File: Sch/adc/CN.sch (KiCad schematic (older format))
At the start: 8 parts, among them J1 JP4, J2 Header5, P1 CONN_02X40, U1 LTC2292

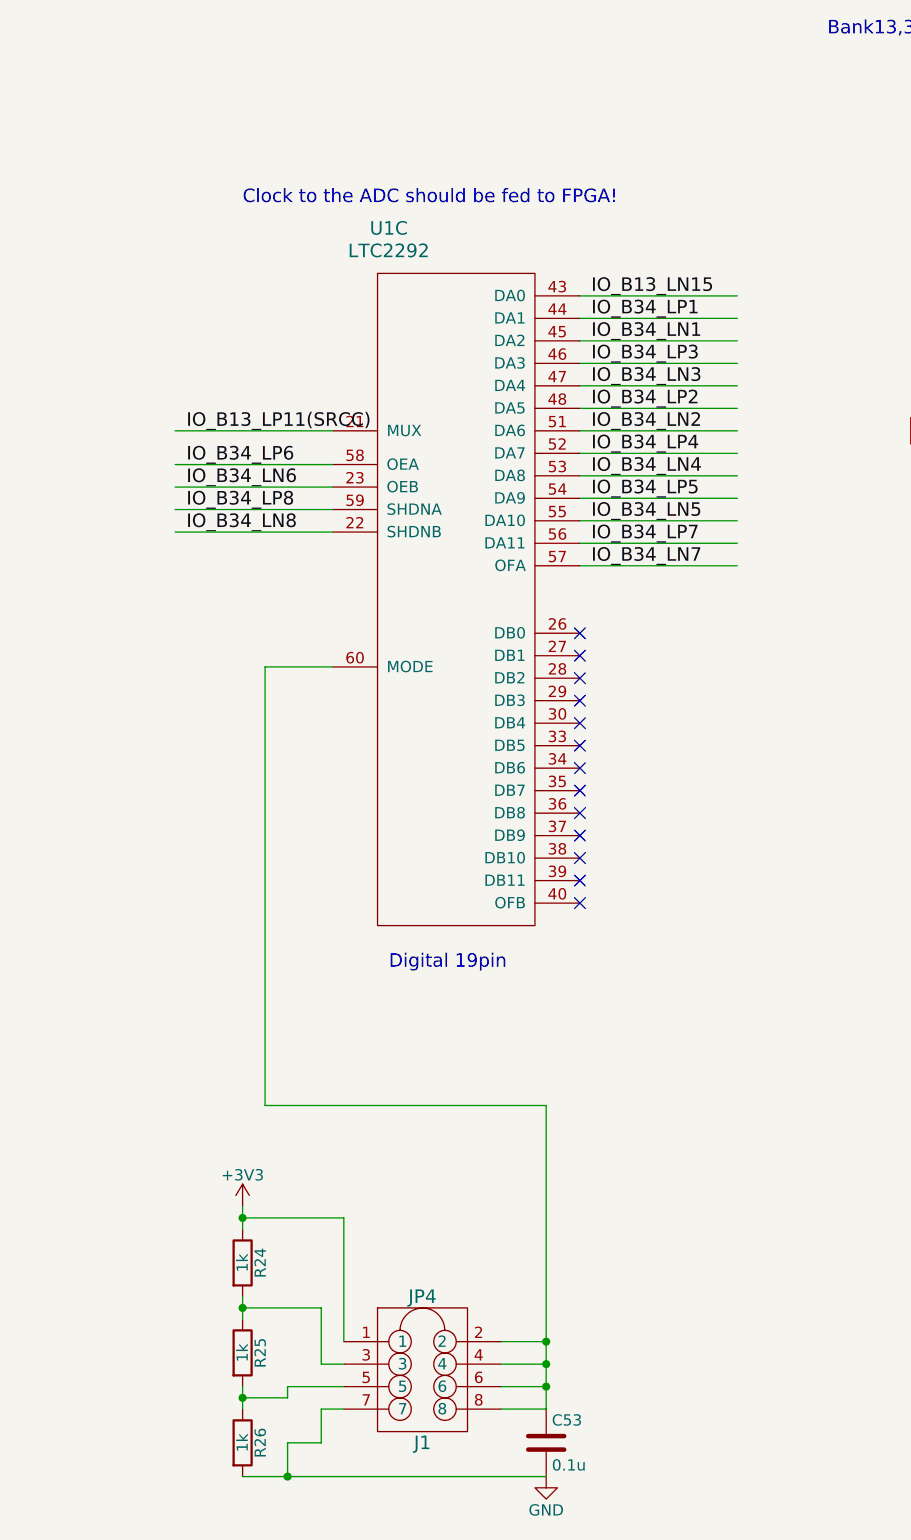
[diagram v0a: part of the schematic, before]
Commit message: Add resistors for ADC out
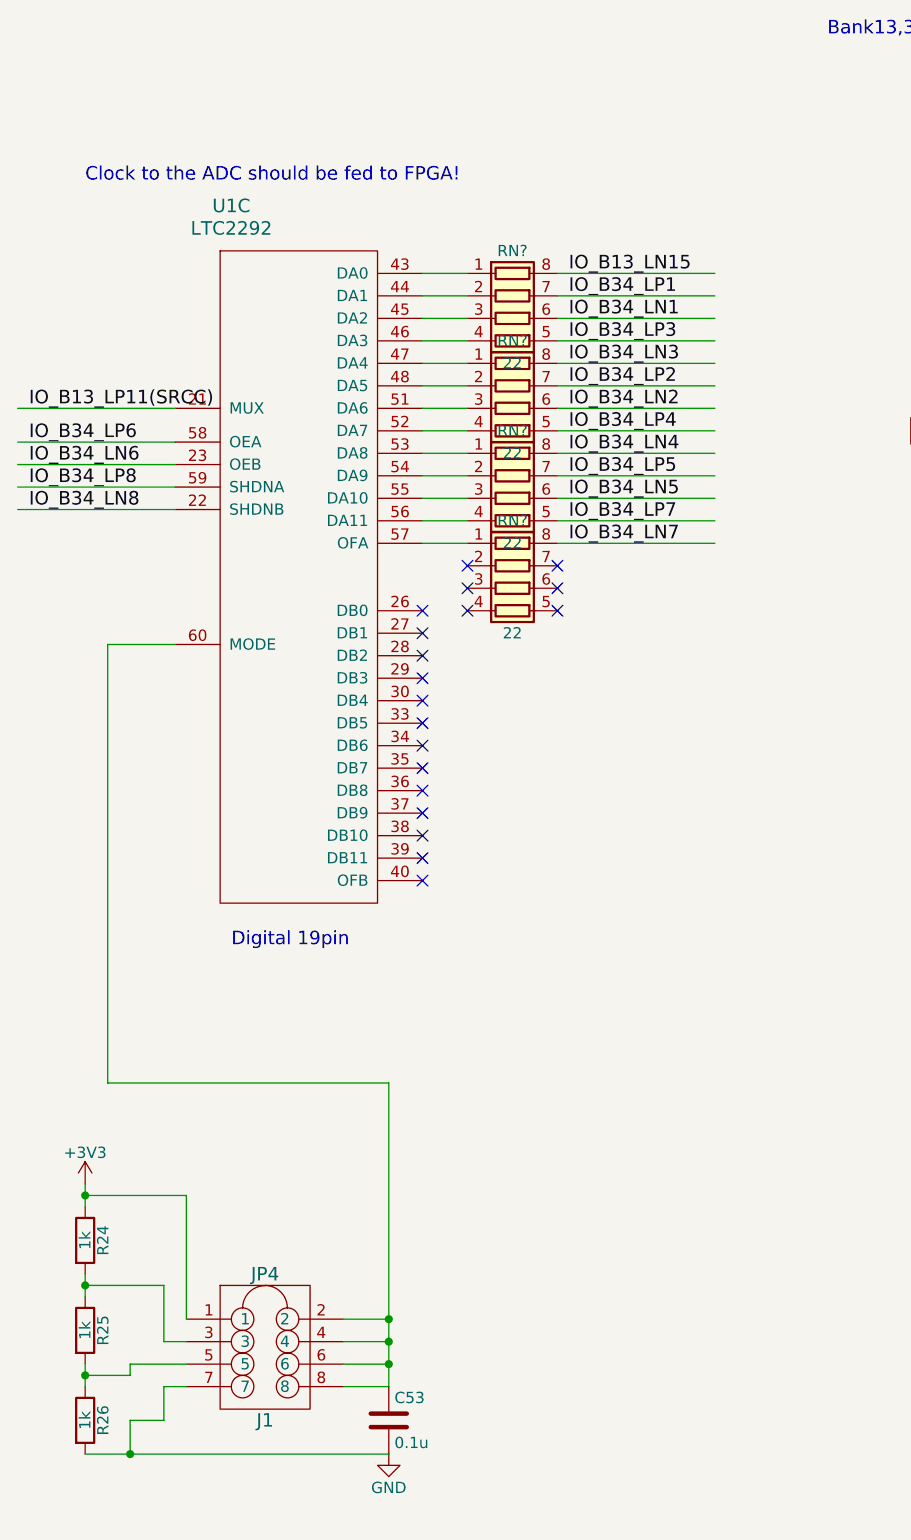
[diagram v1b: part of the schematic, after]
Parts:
- added RN? (x4): 22, symbol R_Pack04
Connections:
- wire segments 96 -> 109
- no-connect marks 55 -> 61
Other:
- moved on the sheet: C53, J1, R24, R25, R26, U1C

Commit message: Almost finished except Audio
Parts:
- gave numbers to parts that had none: 4
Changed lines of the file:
@@
 NoConn ~ 5950 2250
 $Comp
-L R_Pack04 RN?
+L R_Pack04 RN1
 U 1 1 58A5BF52
 P 3700 2050
-F 0 "RN?" V 3400 2050 50  0000 C CNN
+F 0 "RN1" V 3400 2050 50  0000 C CNN
 F 1 "22" V 3900 2050 50  0000 C CNN
 F 2 "" V 3975 2050 50  0001 C CNN
@@
 $EndComp
 $Comp
-L R_Pack04 RN?
+L R_Pack04 RN2
 U 1 1 58A5BFD7
 P 3700 2450
-F 0 "RN?" V 3400 2450 50  0000 C CNN
+F 0 "RN2" V 3400 2450 50  0000 C CNN
 F 1 "22" V 3900 2450 50  0000 C CNN
 F 2 "" V 3975 2450 50  0001 C CNN
@@
 $EndComp
 $Comp
-L R_Pack04 RN?
+L R_Pack04 RN3
 U 1 1 58A5C027
 P 3700 2850
-F 0 "RN?" V 3400 2850 50  0000 C CNN
+F 0 "RN3" V 3400 2850 50  0000 C CNN
 F 1 "22" V 3900 2850 50  0000 C CNN
 F 2 "" V 3975 2850 50  0001 C CNN
@@
 $EndComp
 $Comp
-L R_Pack04 RN?
+L R_Pack04 RN4
 U 1 1 58A5C02D
 P 3700 3250
-F 0 "RN?" V 3400 3250 50  0000 C CNN
+F 0 "RN4" V 3400 3250 50  0000 C CNN
 F 1 "22" V 3900 3250 50  0000 C CNN
 F 2 "" V 3975 3250 50  0001 C CNN

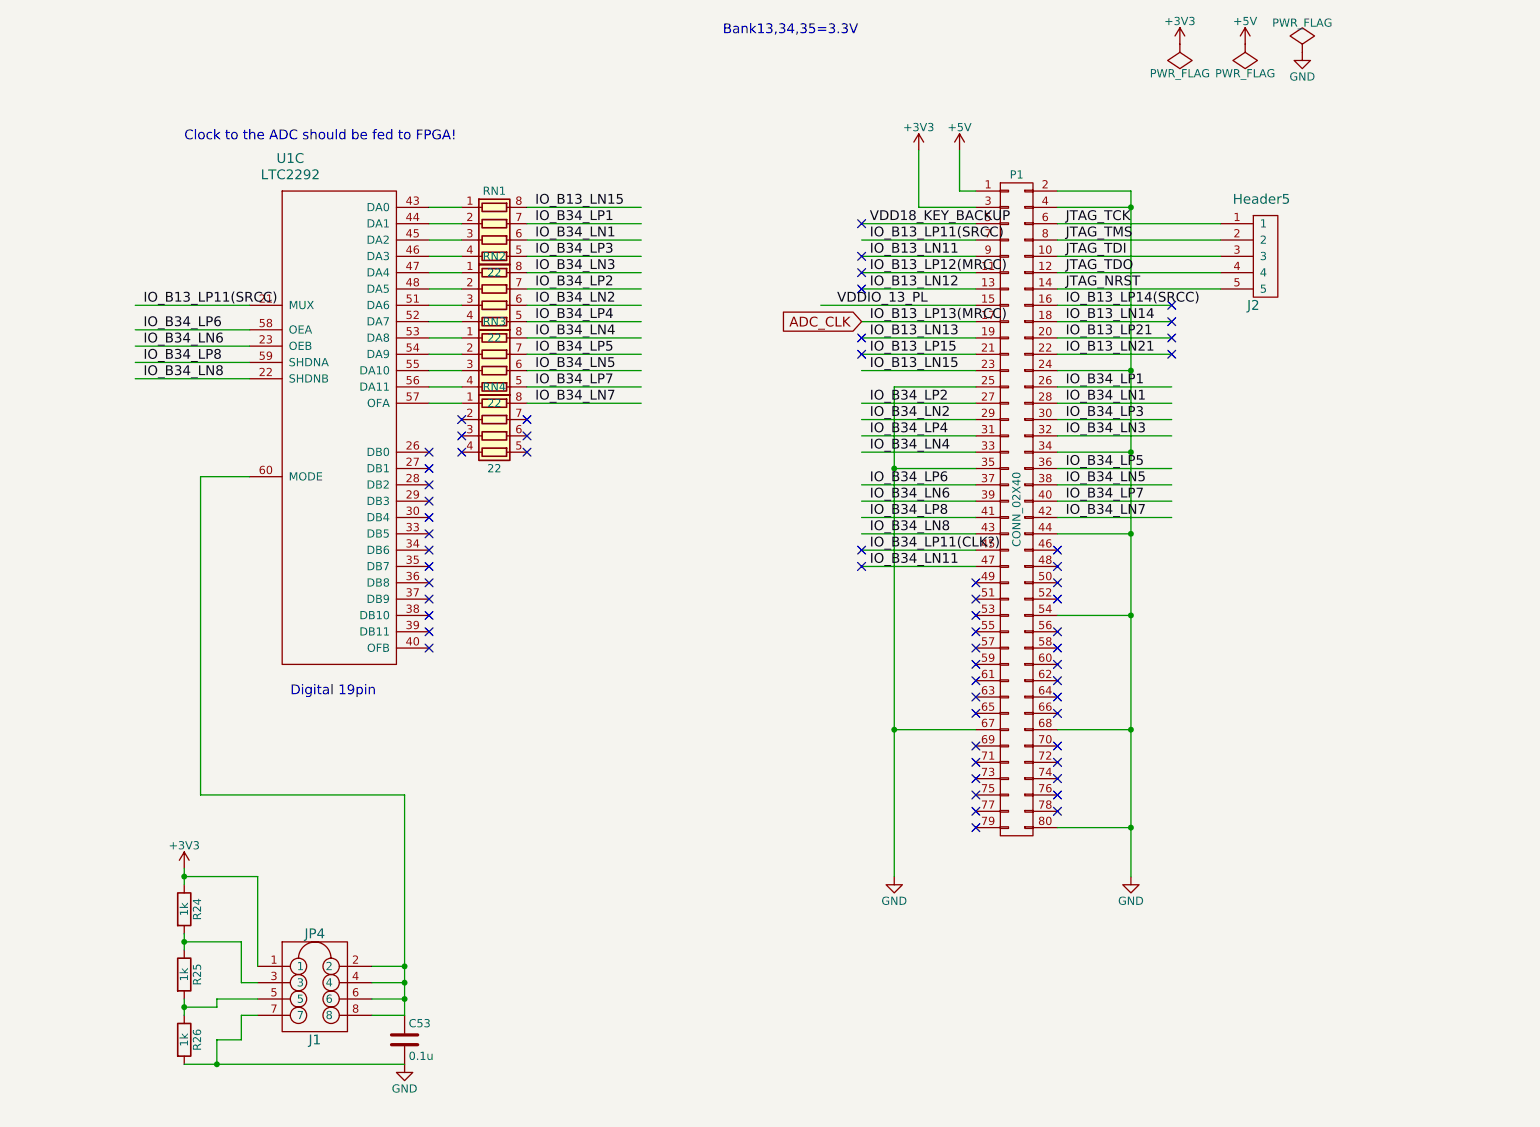
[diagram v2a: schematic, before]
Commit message: Fix MODE pin voltage of the ADC
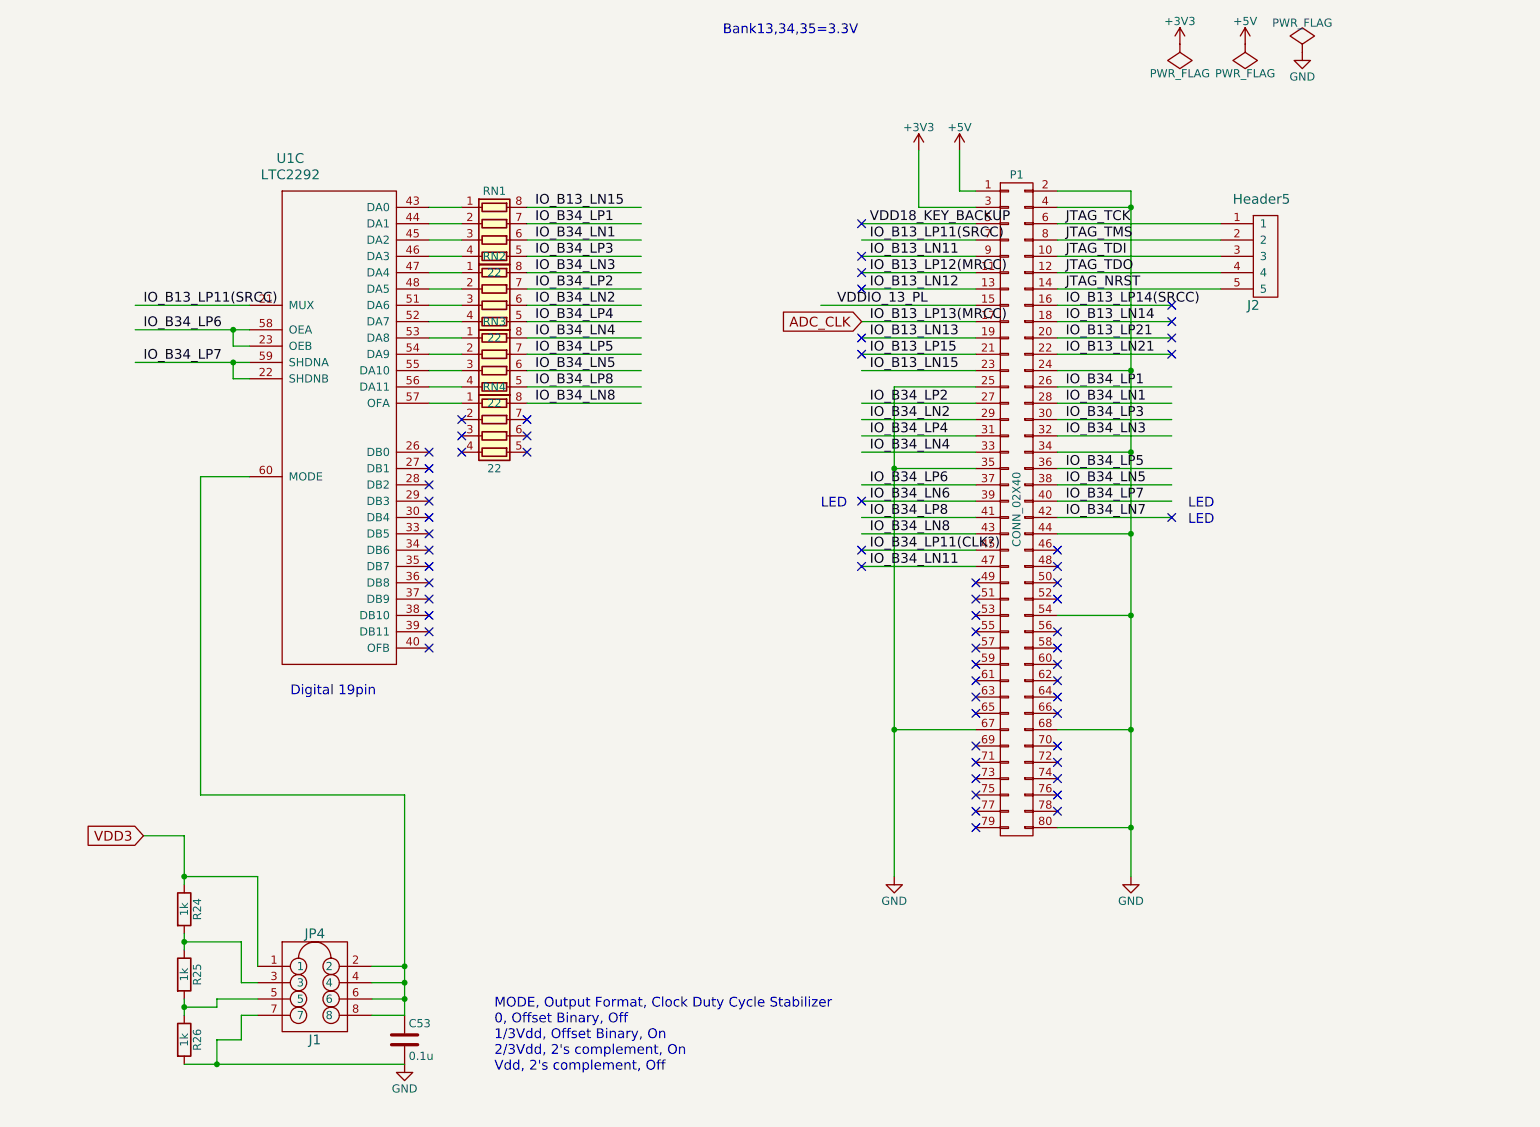
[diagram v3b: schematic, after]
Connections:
- net labels added: VDD3
- wire segments 109 -> 112
- no-connect marks 61 -> 63
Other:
- note added: "LED"
- note added: "MODE, Output Format, Clock Duty Cycle Stabilizer\n0, Offset Binary, Off\n1/3Vdd, Offset Binary, On\n2/3Vdd, 2's complement, On\nVdd, 2's complement, Off"
- note removed: "Clock to the ADC should be fed to FPGA!"
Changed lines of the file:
@@
 NoConn ~ 3300 4450
 NoConn ~ 3300 4550
-Text Notes 1800 1450 0    60   ~ 0
-Clock to the ADC should be fed to FPGA!
 Text Notes 2450 4850 0    60   ~ 0
 Digital 19pin
@@
 IO_B34_LN5
 Text Label 3950 2950 0    60   ~ 0
-IO_B34_LP7
+IO_B34_LP8
 Text Label 3950 3050 0    60   ~ 0
-IO_B34_LN7
+IO_B34_LN8
 Text Label 3950 2650 0    60   ~ 0
 IO_B34_LN4
@@
 Text Label 3950 1850 0    60   ~ 0
 IO_B13_LN15
-Text Label 1550 2900 0    60   ~ 0
-IO_B34_LN8
 Text Label 1550 2800 0    60   ~ 0
-IO_B34_LP8
-Text Label 1550 2700 0    60   ~ 0
-IO_B34_LN6
+IO_B34_LP7
 Text Label 1550 2600 0    60   ~ 0
 IO_B34_LP6
@@
 IO_B13_LP11(SRCC)
 $Comp
-L +3V3 #PWR011
-U 1 1 58A5E943
-P 1800 5900
-F 0 "#PWR011" H 1800 5750 50  0001 C CNN
-F 1 "+3V3" H 1800 6040 50  0000 C CNN
-F 2 "" H 1800 5900 50  0000 C CNN
-F 3 "" H 1800 5900 50  0000 C CNN
-	1    1800 5900
-	1    0    0    -1
-$EndComp
-$Comp
 L R R24
 U 1 1 58A5E977
@@
 $EndComp
 $Comp
-L GND #PWR012
+L GND #PWR011
 U 1 1 58A5EE0A
 P 3150 7100
-F 0 "#PWR012" H 3150 6850 50  0001 C CNN
+F 0 "#PWR011" H 3150 6850 50  0001 C CNN
 F 1 "GND" H 3150 6950 50  0000 C CNN
 F 2 "" H 3150 7100 50  0000 C CNN
@@
 	2200 2600 1500 2600
 Wire Wire Line
-	2200 2700 1500 2700
-Wire Wire Line
 	2200 2800 1500 2800
 Wire Wire Line
-	2200 2900 1500 2900
-Wire Wire Line
 	2200 2450 1500 2450
 Wire Wire Line
-	1800 5900 1800 6000
+	1800 5700 1800 6000
 Wire Wire Line
 	1800 6300 1800 6400
@@
 NoConn ~ 3900 3250
 NoConn ~ 3900 3150
+Wire Wire Line
+	2100 2800 2100 2900
+Wire Wire Line
+	2100 2900 2200 2900
+Connection ~ 2100 2800
+Wire Wire Line
+	2100 2600 2100 2700
+Wire Wire Line
+	2100 2700 2200 2700
+Connection ~ 2100 2600
+Text Notes 7950 3800 0    60   ~ 0
+LED
+Text Notes 7950 3700 0    60   ~ 0
+LED
+Text Notes 5700 3700 0    60   ~ 0
+LED
+NoConn ~ 5950 3650
+NoConn ~ 7850 3750
+Text Notes 3700 7150 0    60   ~ 0
+MODE, Output Format, Clock Duty Cycle Stabilizer\n0, Offset Binary, Off\n1/3Vdd, Offset Binary, On\n2/3Vdd, 2's complement, On\nVdd, 2's complement, Off
+Text GLabel 1550 5700 0    60   Input ~ 0
+VDD3
+Wire Wire Line
+	1550 5700 1800 5700
 $EndSCHEMATC

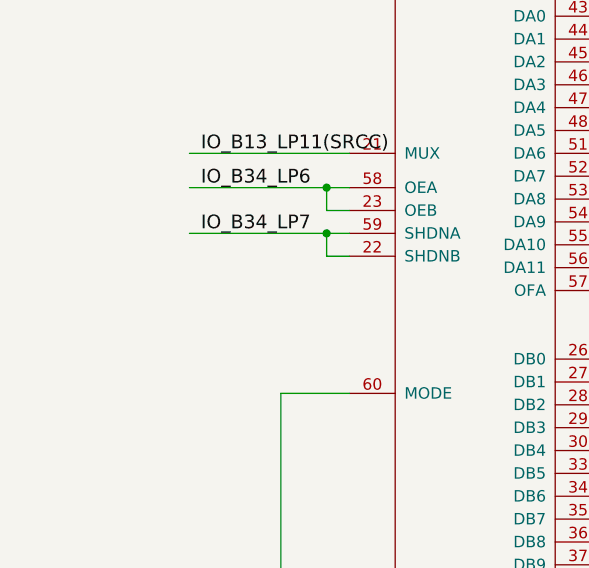
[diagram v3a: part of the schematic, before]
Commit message: Select nap mode for each channel
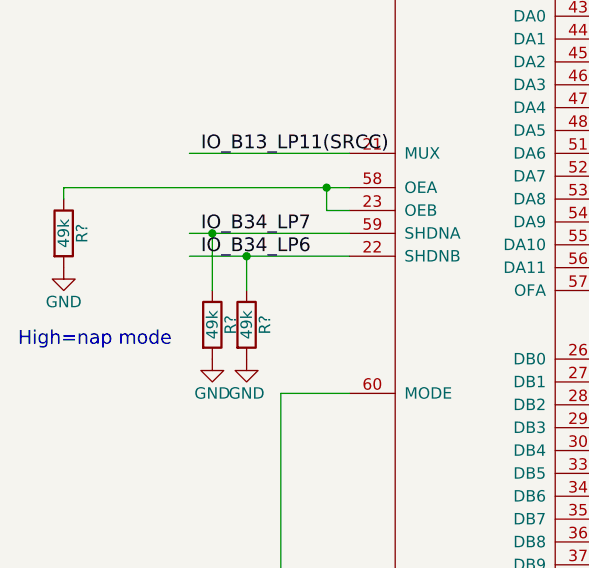
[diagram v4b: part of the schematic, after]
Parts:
- added R? (x3): 49k, symbol R
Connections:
- wire segments 112 -> 114
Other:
- note added: "High=nap mode"

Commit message: DAC in progress
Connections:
- net labels added: BCLK, DACIN, FS
- no-connect marks 63 -> 60
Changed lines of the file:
@@
 $Descr A4 11693 8268
 encoding utf-8
-Sheet 2 3
+Sheet 2 4
 Title ""
 Date ""
@@
 $EndComp
 NoConn ~ 7850 2450
-NoConn ~ 7850 2550
-NoConn ~ 7850 2650
-NoConn ~ 7850 2750
 NoConn ~ 5950 1950
 NoConn ~ 5950 2150
@@
 Text Notes 750  3300 0    60   ~ 0
 High=nap mode
+Text GLabel 7850 2550 2    60   Output ~ 0
+FS
+Text GLabel 7850 2650 2    60   Output ~ 0
+BCLK
+Text GLabel 7850 2750 2    60   Output ~ 0
+DACIN
 $EndSCHEMATC

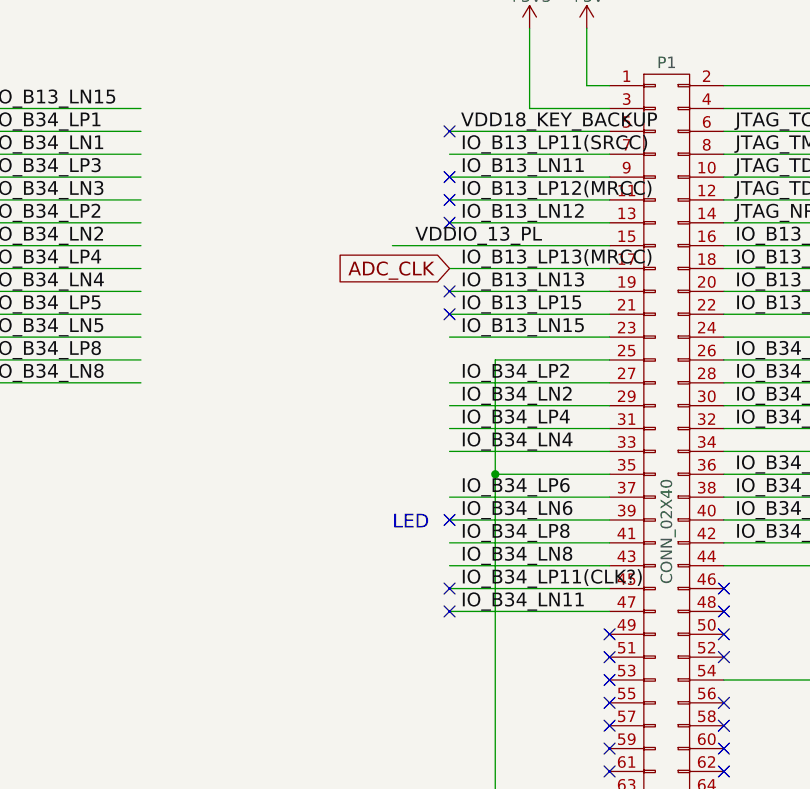
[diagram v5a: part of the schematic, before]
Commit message: Audio DAC almost done. Is it OK to set VDDC=3.3V?
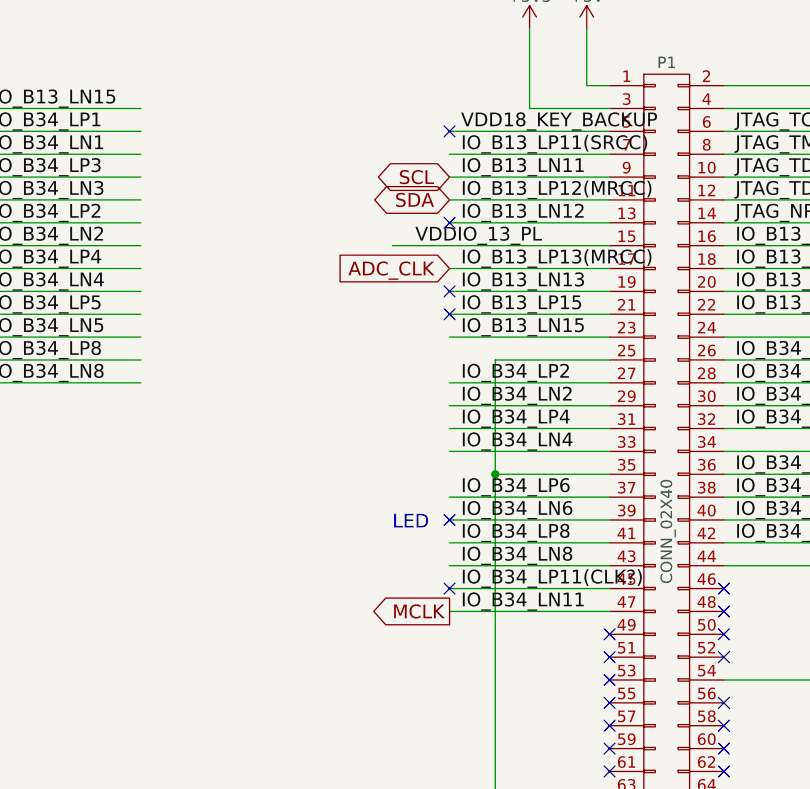
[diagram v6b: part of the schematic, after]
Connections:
- net labels added: MCLK, SCL, SDA
- no-connect marks 60 -> 57
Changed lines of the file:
@@
 IO_B34_LP6
 NoConn ~ 5950 3950
-NoConn ~ 5950 4050
 Text Notes 5100 800  0    60   ~ 0
 Bank13,34,35=3.3V
@@
 NoConn ~ 7850 2450
 NoConn ~ 5950 1950
-NoConn ~ 5950 2150
 NoConn ~ 5950 2350
 NoConn ~ 5950 2650
@@
 Text GLabel 5950 2550 0    60   Input ~ 0
 ADC_CLK
-NoConn ~ 5950 2250
 $Comp
 L R_Pack04 RN1
@@
 Text GLabel 7850 2750 2    60   Output ~ 0
 DACIN
+Text GLabel 5950 4050 0    60   Output ~ 0
+MCLK
+Text GLabel 5950 2150 0    60   BiDi ~ 0
+SCL
+Text GLabel 5950 2250 0    60   BiDi ~ 0
+SDA
 $EndSCHEMATC
